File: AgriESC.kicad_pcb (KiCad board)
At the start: 2 copper layers, 94.6 x 69.2 mm, 310 parts, among them J1 SUPPLY, J10 GPIO, J11 USB_OTG, J12 HALL_ENC, J2 PH_A, J3 PH_B, J4 PH_C, J6 COMM, J7 SERVO, J8 CAN, J9 SWD, SW1 SW_SPDT, U1 FDMS7698, U10 STM32F405RGT6, U11 DRV8303, U12 TJA1051TK-3, U13 LMR16006YQ, U14 MCP1700-3302E_SOT23, U15 MCP1700-3302E_SOT23, U2 FDMS7698, U3 FDMS7698, U4 FDMS7698, U5 FDMS7698, U6 FDMS7698, U7 MAX9920, U8 MAX9920, U9 MAX9920, Y1 8M Resonator

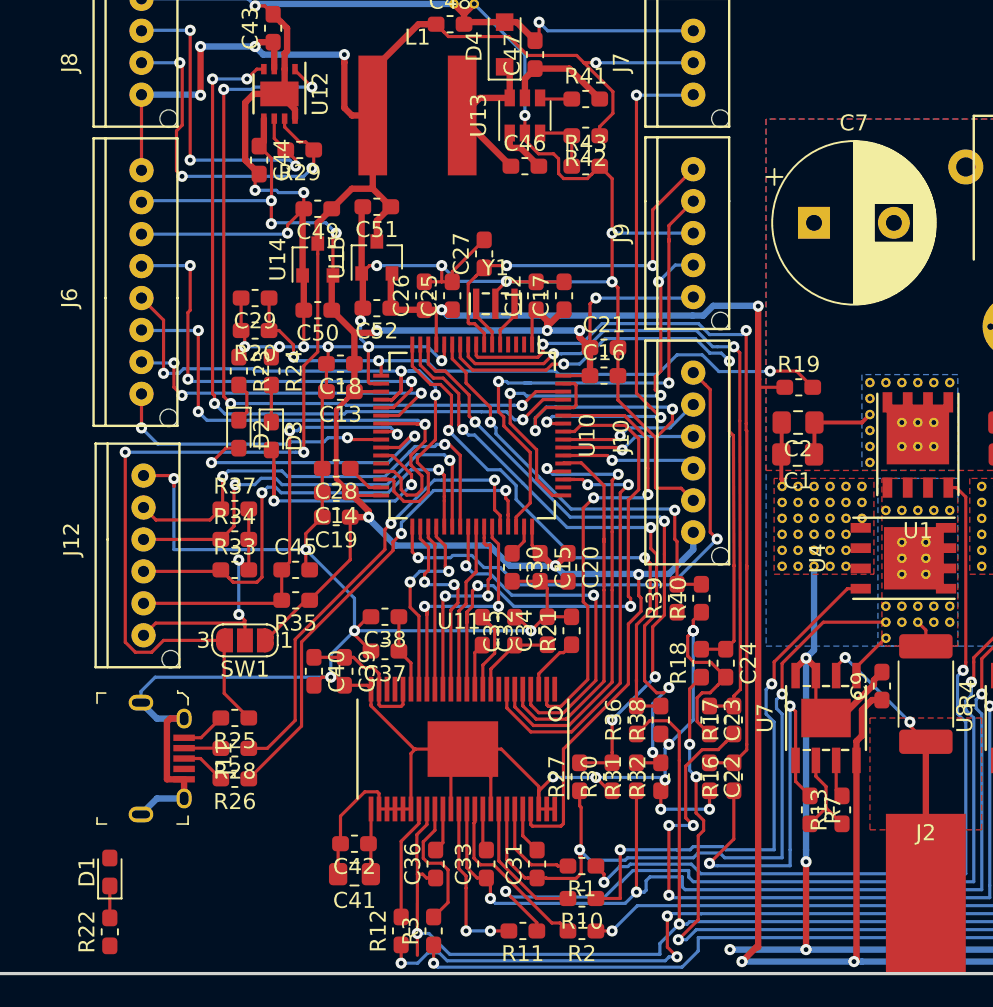
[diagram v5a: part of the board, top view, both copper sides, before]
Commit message: Routing completed! Now cleaning up tracks and increasing width where appropriate
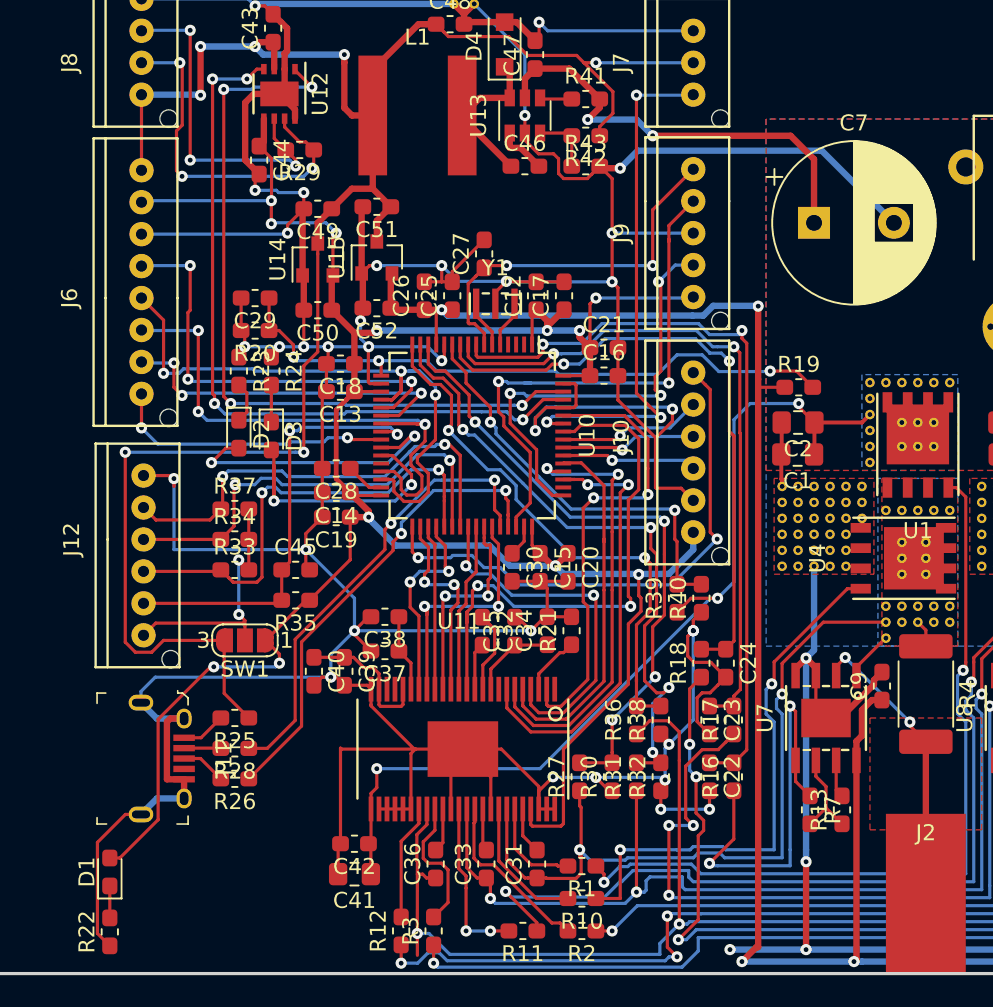
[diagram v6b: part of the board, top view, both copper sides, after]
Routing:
- net SUPPLY: track 27.2 -> 97.0 mm, vias 0 -> 5
- net SL_A: track 520.0 -> 555.9 mm, vias 43 -> 44
- net VCC: track 137.5 -> 158.6 mm, vias 10 -> 12

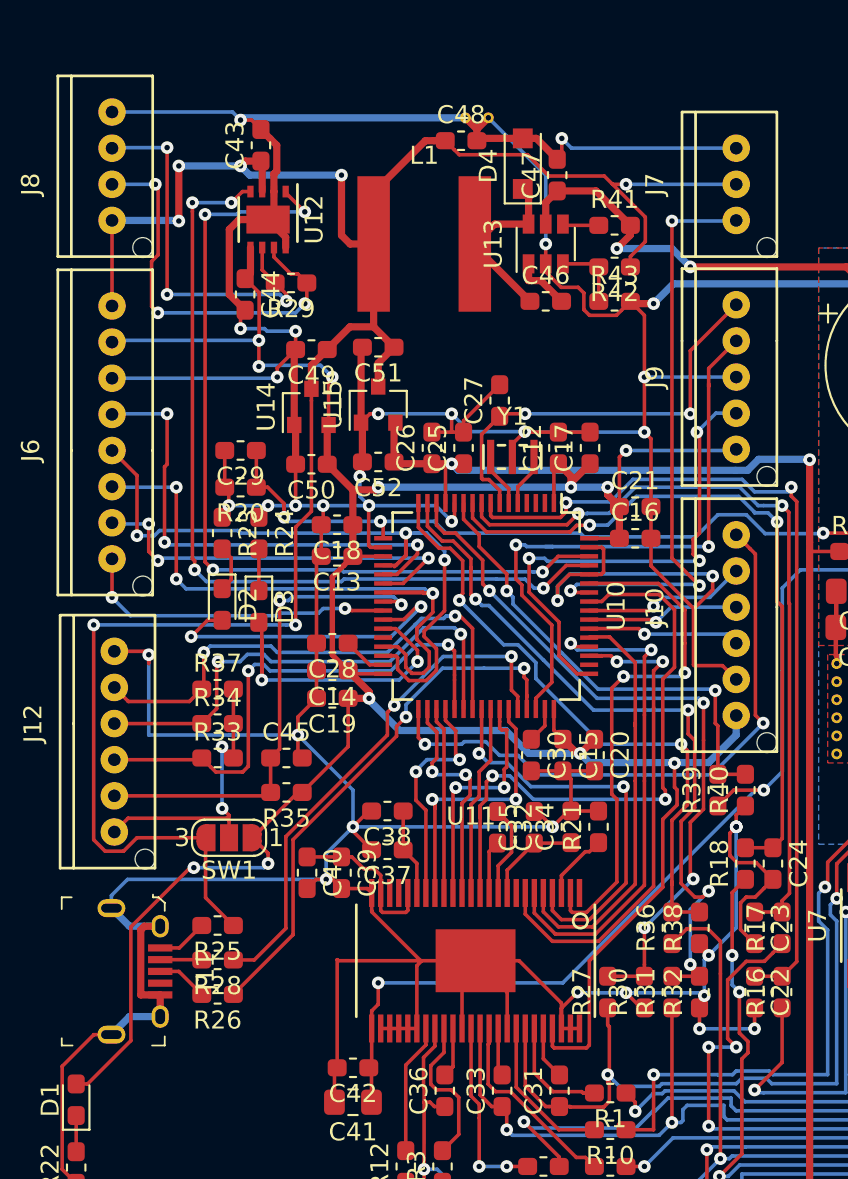
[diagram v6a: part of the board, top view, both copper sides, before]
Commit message: Widening important traces
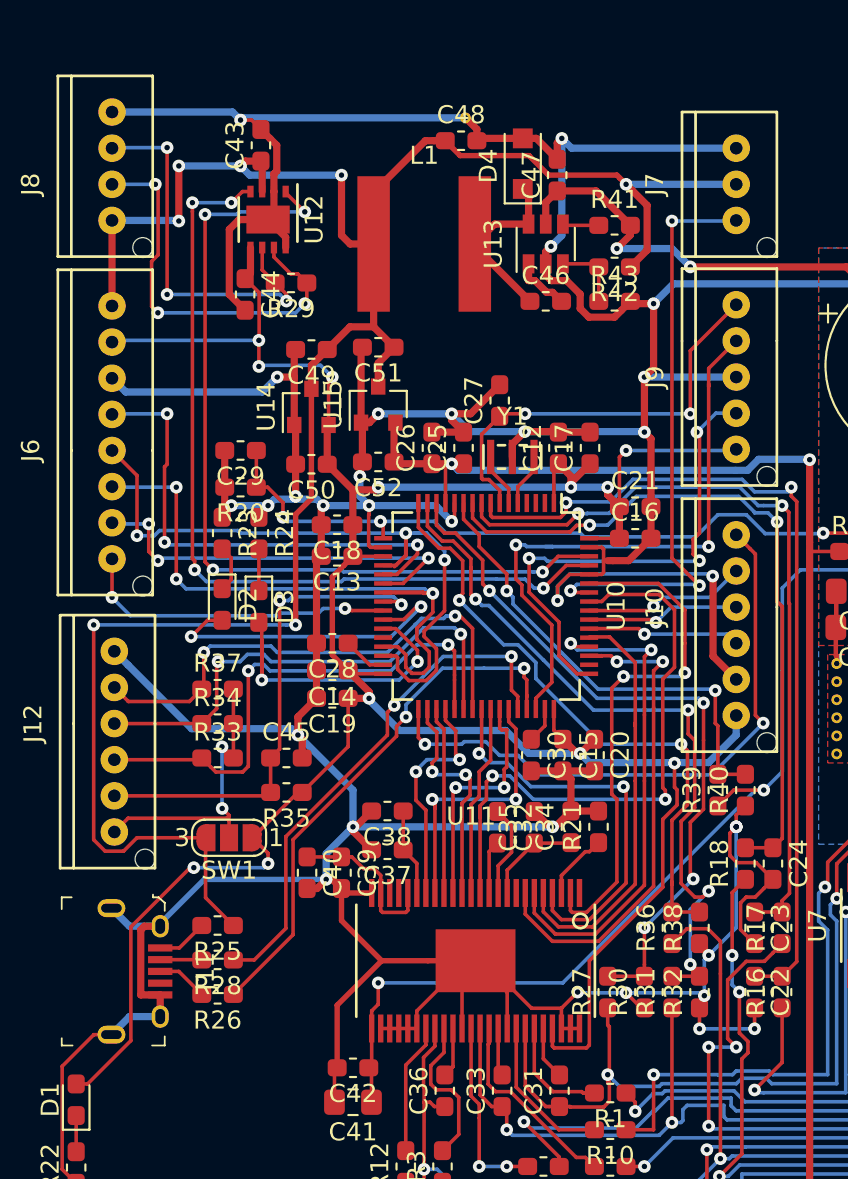
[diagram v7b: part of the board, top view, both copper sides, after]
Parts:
- removed the REF** at (93.5, -5.21)
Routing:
- net SL_A: track 555.9 -> 538.7 mm, vias 44 -> 41

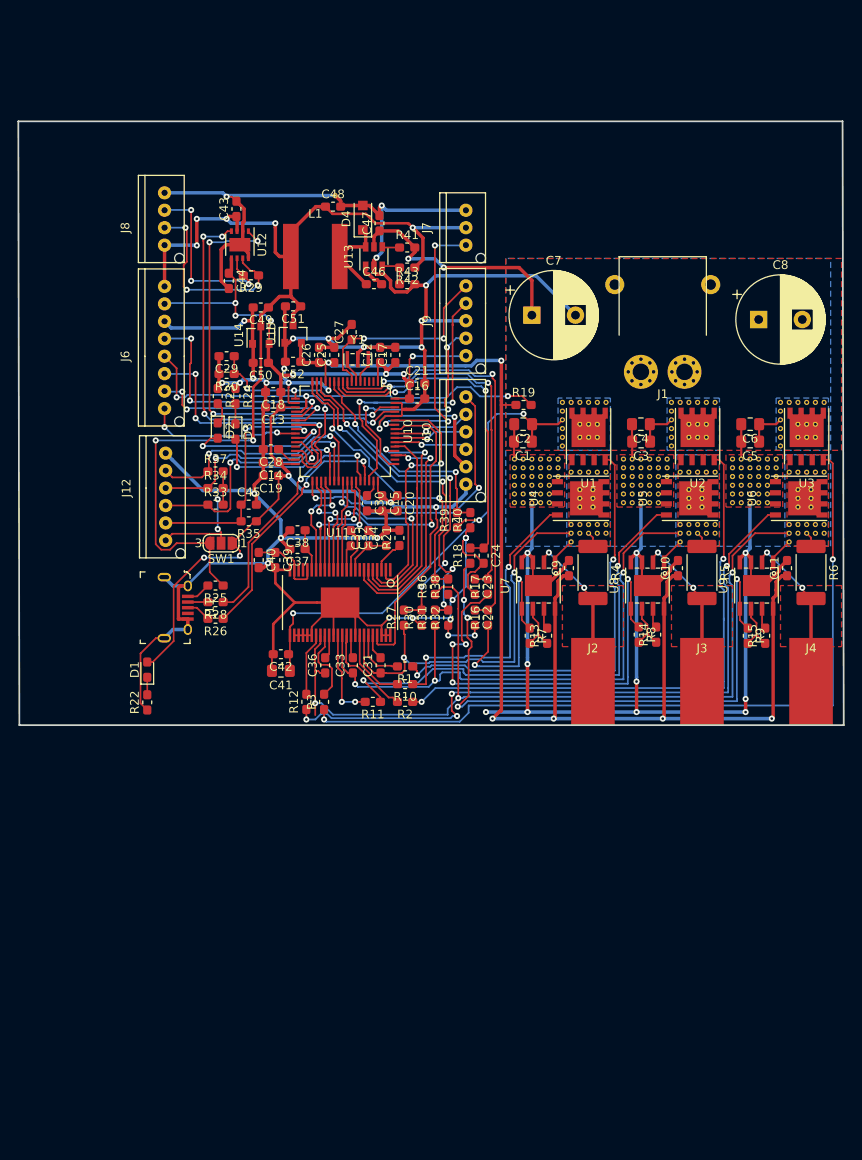
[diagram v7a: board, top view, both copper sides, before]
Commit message: Correcting boundary
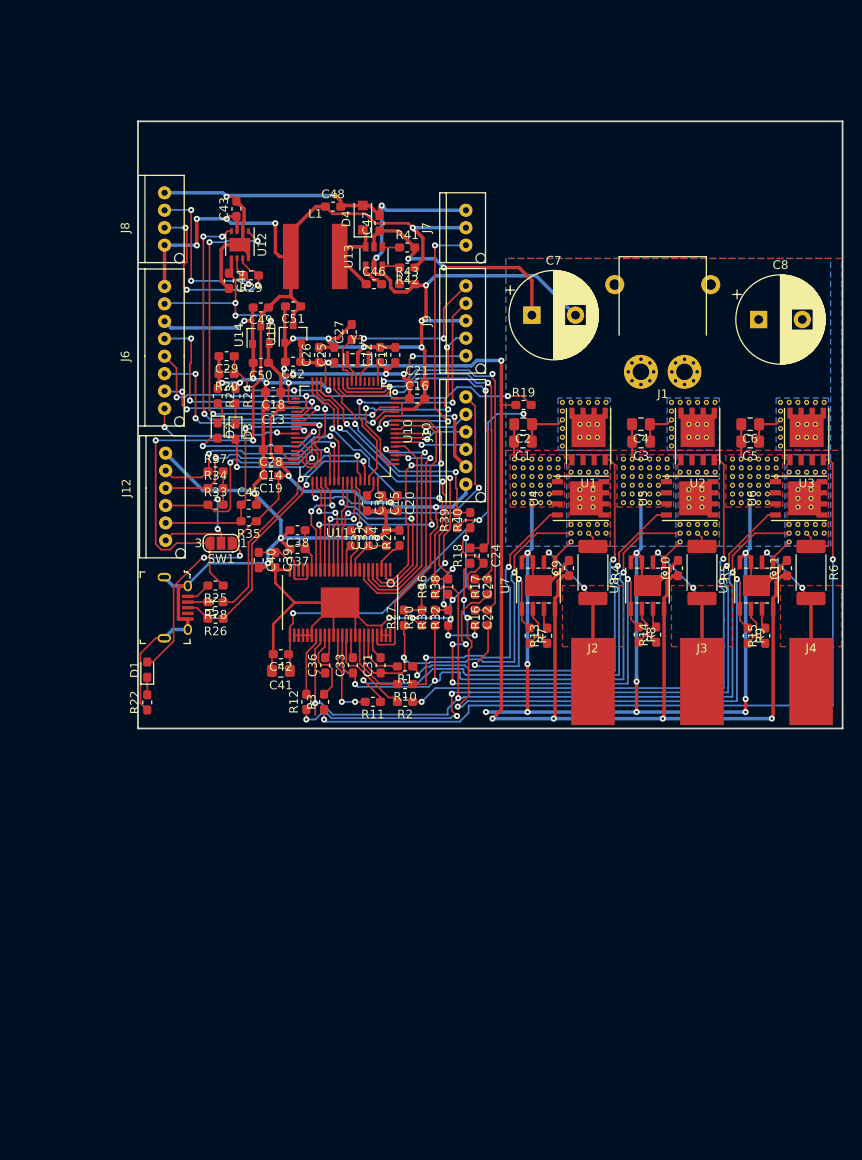
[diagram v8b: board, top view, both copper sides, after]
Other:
- board size 94.6 x 69.2 mm -> 80.8 x 69.6 mm
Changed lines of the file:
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@@
     )
   )
-  (gr_line (start 150.368 -13.716) (end 150.5 55.5) (layer Edge.Cuts) (width 0.2))
-  (gr_line (start 55.88 -13.716) (end 150.368 -13.716) (layer Edge.Cuts) (width 0.2))
-  (gr_line (start 56 55.5) (end 55.88 -13.716) (layer Edge.Cuts) (width 0.2))
-  (gr_line (start 150.5 55.5) (end 56 55.5) (layer Edge.Cuts) (width 0.2))
+  (gr_line (start 150.368 -13.716) (end 150.368 55.88) (layer Edge.Cuts) (width 0.2))
+  (gr_line (start 69.596 -13.716) (end 150.368 -13.716) (layer Edge.Cuts) (width 0.2))
+  (gr_line (start 69.596 55.88) (end 69.596 -13.716) (layer Edge.Cuts) (width 0.2))
+  (gr_line (start 150.368 55.88) (end 69.596 55.88) (layer Edge.Cuts) (width 0.2))
   (segment (start 112.725 22.975) (end 112.7 23) (width 0.25) (layer F.Cu) (net 1) (status 30))
   (segment (start 112.725 21) (end 112.725 22.975) (width 0.25) (layer F.Cu) (net 1) (status 30))
